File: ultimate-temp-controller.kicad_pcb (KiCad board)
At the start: 2 copper layers, 80 x 100 mm, 74 parts, among them CON1 SD_Card, IC1 ATMEGA328-A, P1 ISP, P10 RS485, P2 BUTTONS, P3 OPEN_DRAIN, P4 POWER, P5 I2C1, P6 I2C2, P7 CONN_01X05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

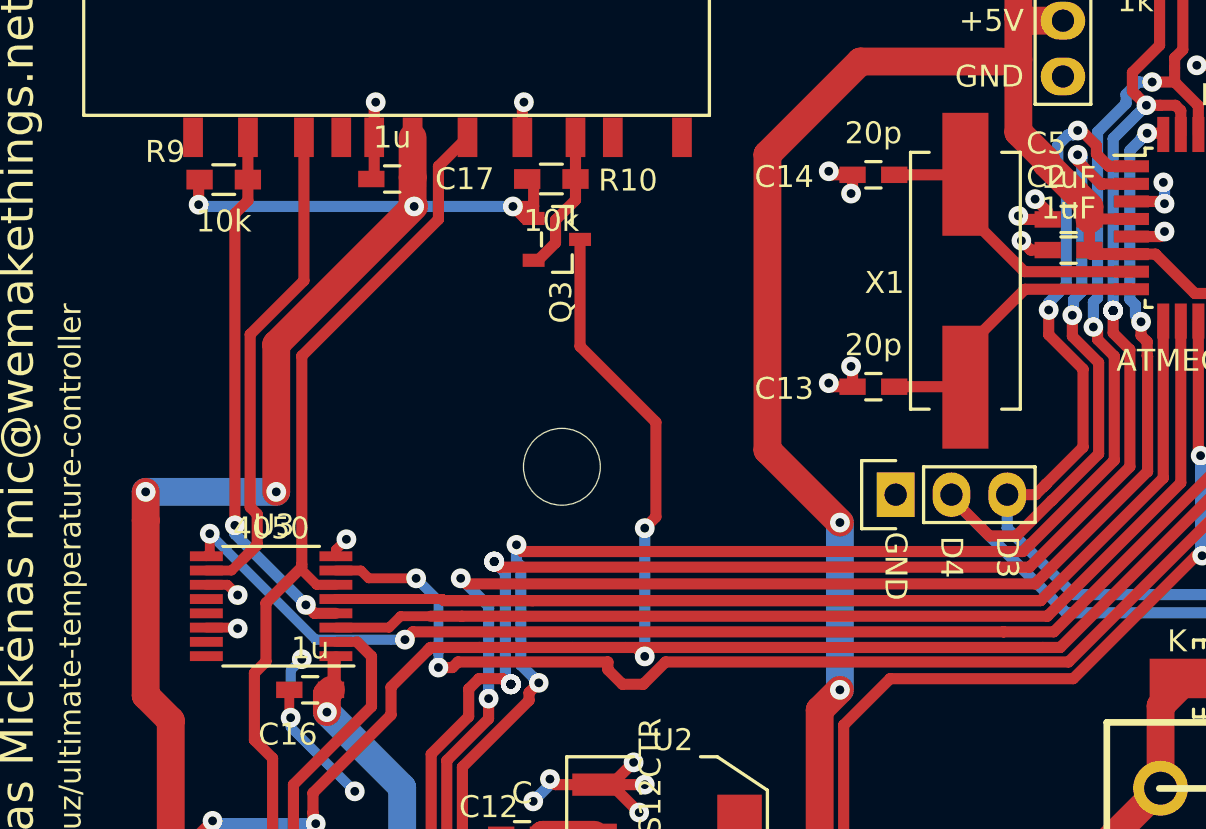
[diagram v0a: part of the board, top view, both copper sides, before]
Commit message: Optimise some tracks
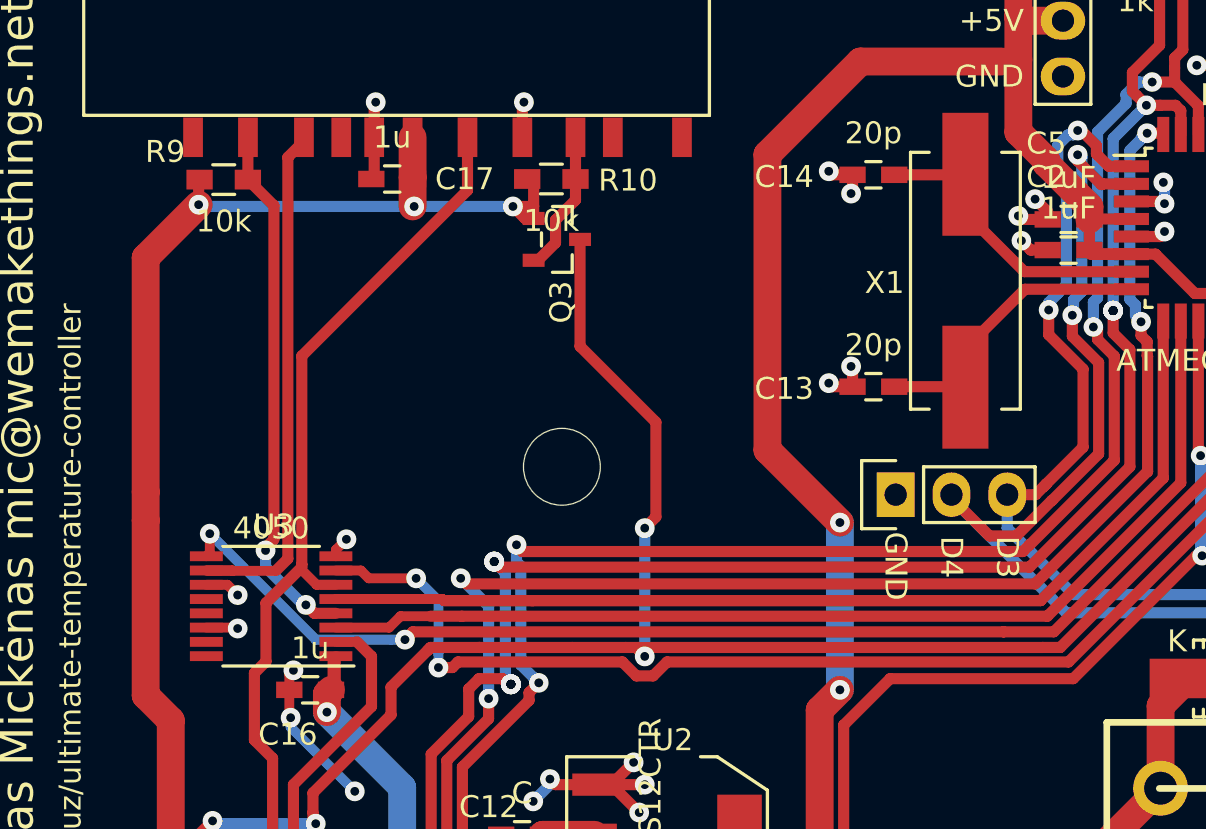
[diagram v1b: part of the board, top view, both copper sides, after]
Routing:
- net +3V3: track 128.1 -> 120.7 mm, vias 14 -> 12
- net /controller/MOSI_3V3: track 22.5 -> 24.6 mm
- net (no net): track 1.91 -> 0.00 mm, vias 1 -> 0
- net GND: track 78.8 -> 79.8 mm, vias 46 -> 47
- net /controller/CLK: track 66.0 -> 65.5 mm

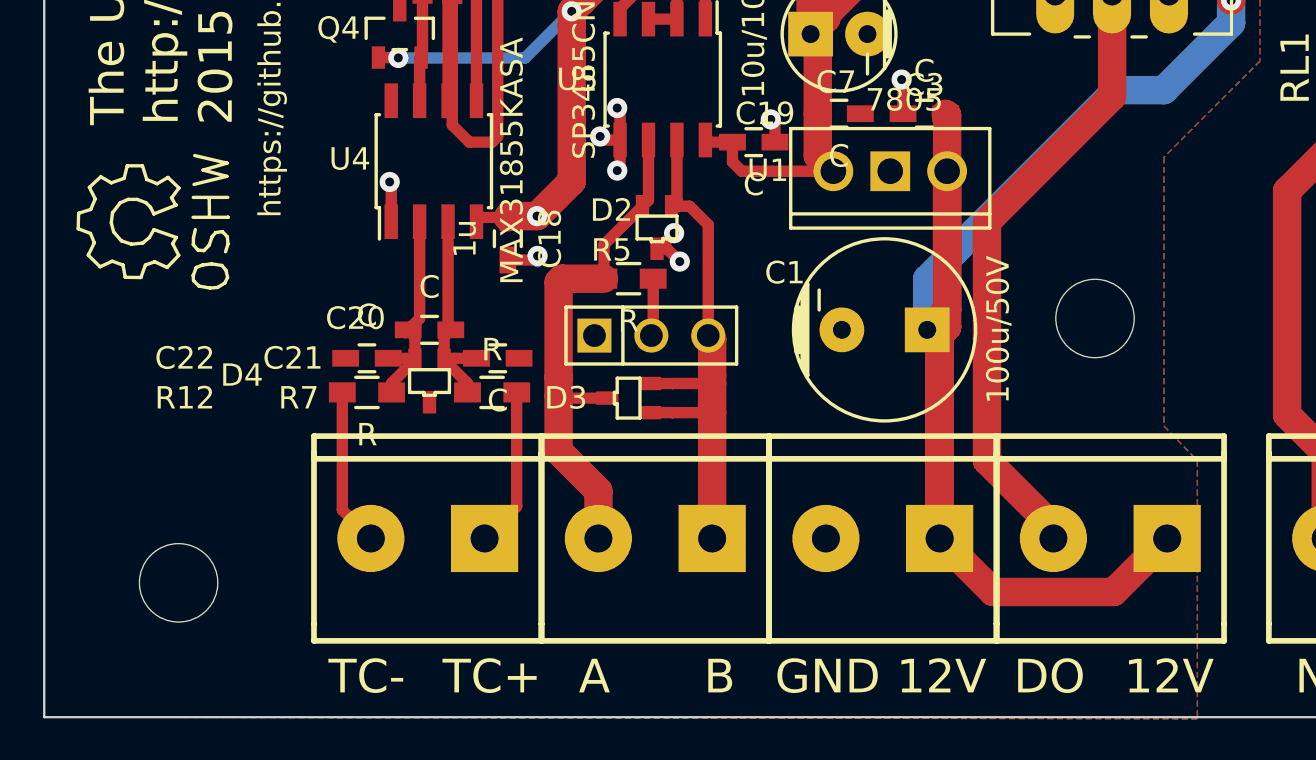
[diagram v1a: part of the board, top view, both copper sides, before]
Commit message: Change TVS diode footprints to SOT-23
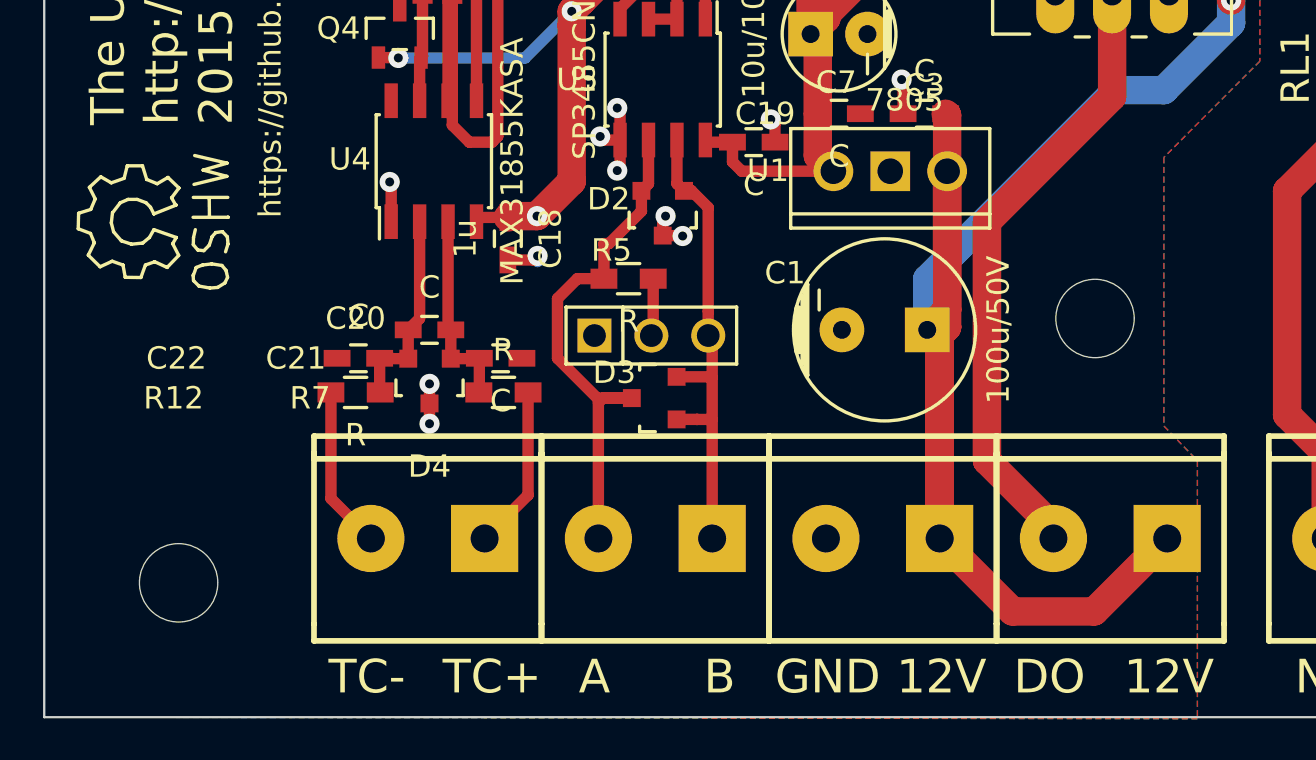
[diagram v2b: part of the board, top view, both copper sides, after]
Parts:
- D2, D3, D4: footprint SMD_Packages:SOT-323 -> Housings_SOT-23_SOT-143_TSOT-6:SOT-23
- moved D3 1.14 mm to (118.2, 174.8), turned to 90 degrees
- moved D2 0.68 mm to (118.6, 166.5), turned to 180 degrees
- moved R12 0.51 mm to (104.9, 174.5)
- moved R7 0.51 mm to (111.5, 174.5)
- moved C22 0.38 mm to (105.0, 173.0)
- moved C21 0.13 mm to (111.4, 173.0)
- turned D4 to 180 degrees
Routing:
- net /controller/RS485B: track 25.0 -> 21.8 mm
- net GND: track 79.8 -> 81.1 mm, vias 47 -> 49
- net Net-(C20-Pad1): track 9.71 -> 8.98 mm
- net VCC: track 88.6 -> 89.3 mm
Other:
- board text added: "TODO: -rezistorių ant CLK ir MOSI linijų? - patikrinti SD kortelės footprintą"
- board text removed: "TODO: - TVS diodu footprintai SC-70, tuo tarpu, kai nusipirkau sot-23 - pakeist MCU i 328P, kad būtų arduino -rezistorių ant CLK ir MOSI linijų? - patikrinti SD kortelės footprintą"

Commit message: Fix netlist problem - update custom tuded ICs: U3 power connections are visible, U5 pin ordering more convenient. Saved cymbol changes to the local cache, not clear if this will help thoug..
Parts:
- IC1: value ATMEGA328-A -> ATMEGA328P-A
- RLY1: renamed from RL1; value FINDER-40.51 -> RELAY_40.61
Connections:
- C1 pad 1: VCC -> +12V
- C3 pad 1: VCC -> +12V
- D1 pad 2: VCC -> +12V
- D4 pad 1: Net-(C20-Pad1) -> Net-(C20-Pad2)
- D4 pad 2: Net-(C20-Pad2) -> Net-(C20-Pad1)
- P3 pad 1: VCC -> +12V
- P4 pad 1: VCC -> +12V
- RLY1 pad 1: VCC -> Net-(D1-Pad1)
- RLY1 pad 2: Net-(D1-Pad1) -> +12V
- U1 pad VI: VCC -> +12V
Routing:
- net +12V: track 0.00 -> 89.3 mm, vias 0 -> 1
- net VCC: track 89.3 -> 0.00 mm, vias 1 -> 0
- net Net-(C20-Pad1): track 8.98 -> 7.72 mm
- net Net-(C20-Pad2): track 9.33 -> 10.6 mm

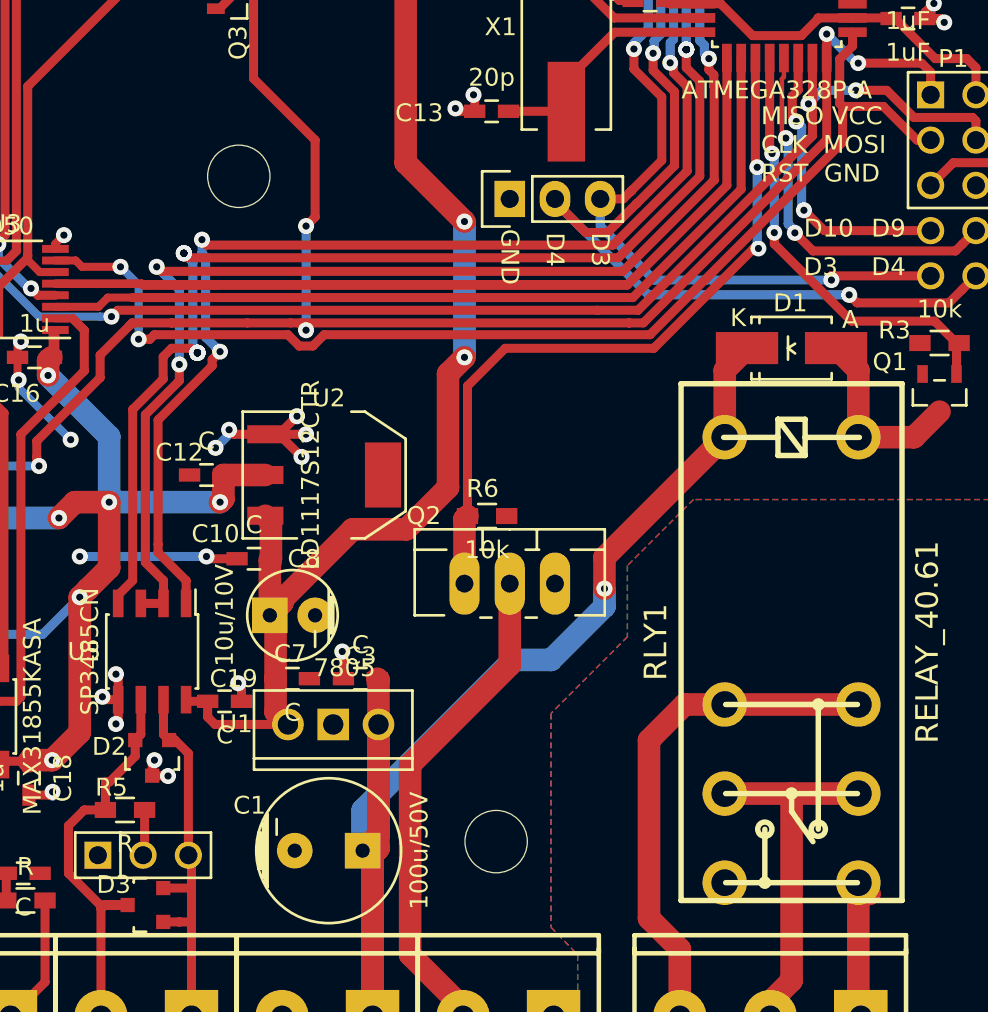
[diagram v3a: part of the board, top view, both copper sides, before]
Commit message: Swap TVS pins again. Add pullup resistors to CS lines.
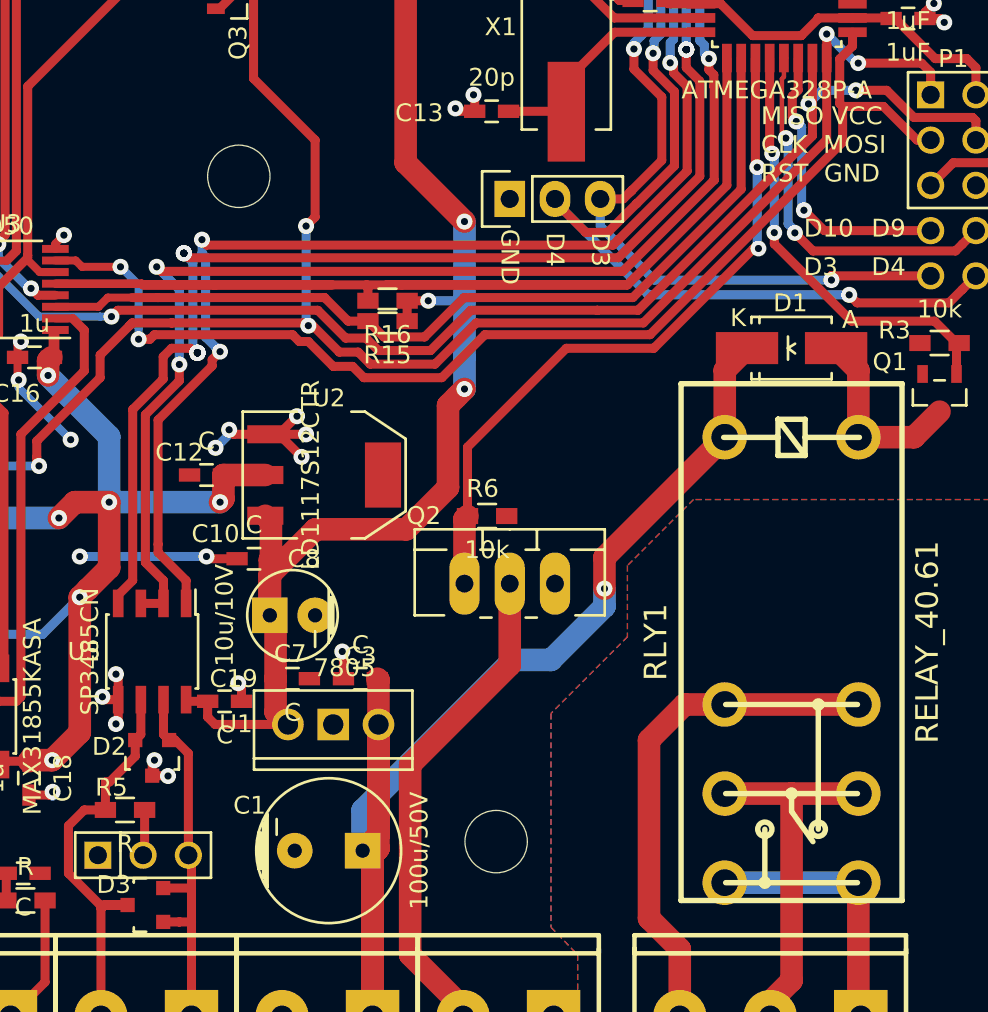
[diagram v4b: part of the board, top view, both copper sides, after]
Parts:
- added R15: 10k, Resistors_SMD:R_0603_HandSoldering, F.Cu at (131.8, 142.0)
- added R16: 10k, Resistors_SMD:R_0603_HandSoldering, F.Cu at (131.8, 140.8)
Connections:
- D4 pad 1: Net-(C20-Pad2) -> Net-(C20-Pad1)
- D4 pad 2: Net-(C20-Pad1) -> Net-(C20-Pad2)
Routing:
- net /controller/RELAY_NO: track 8.47 -> 15.3 mm
- net +5V: track 159.2 -> 164.8 mm, vias 2 -> 3
- net /controller/TRANSISTOR_ON: track 40.4 -> 38.4 mm
- net /controller/CS_SD: track 79.4 -> 77.4 mm
- net /controller/MOSI: track 72.0 -> 73.8 mm
- net /controller/CS_TC: track 48.6 -> 50.4 mm
- net /controller/CLK: track 65.5 -> 67.0 mm
- net Net-(C20-Pad1): track 7.72 -> 8.98 mm
- net Net-(C20-Pad2): track 10.6 -> 9.33 mm
- net /controller/MISO: track 105.9 -> 107.1 mm

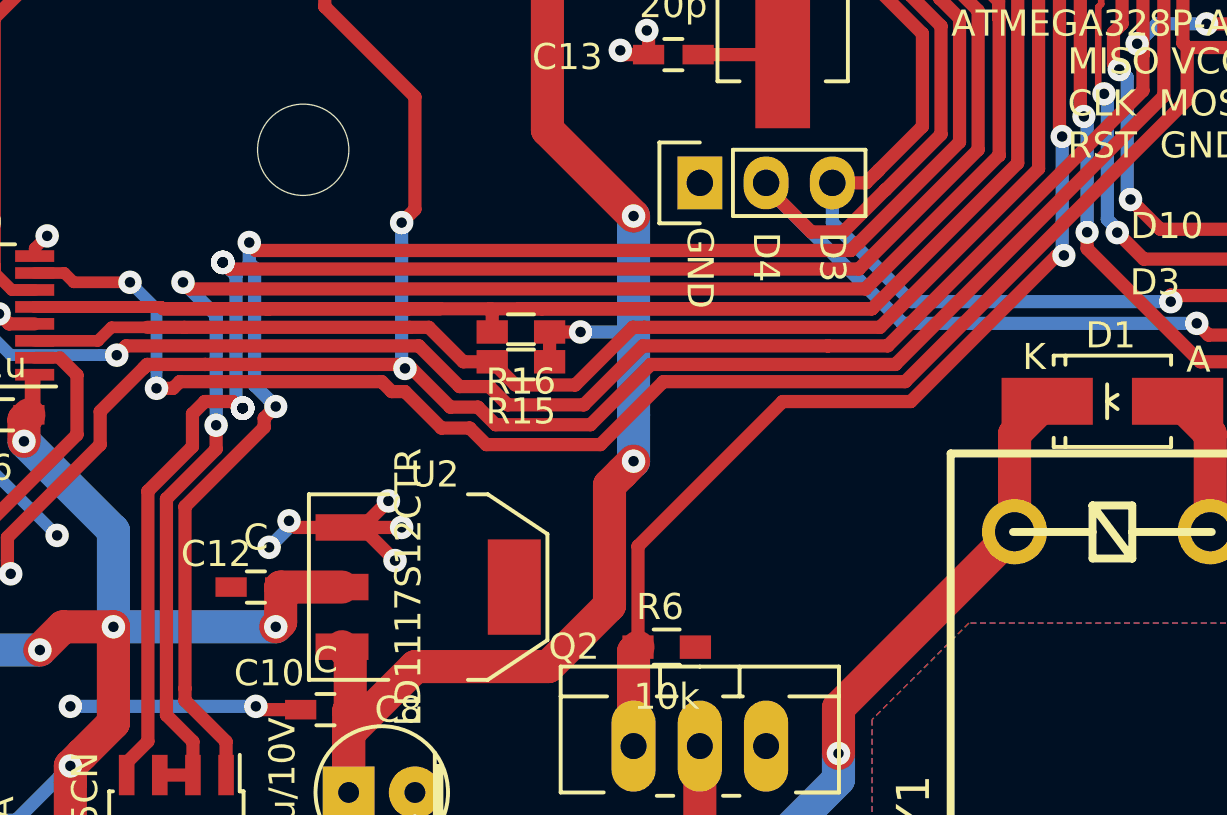
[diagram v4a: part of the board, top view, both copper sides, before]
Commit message: Optimise some tracks
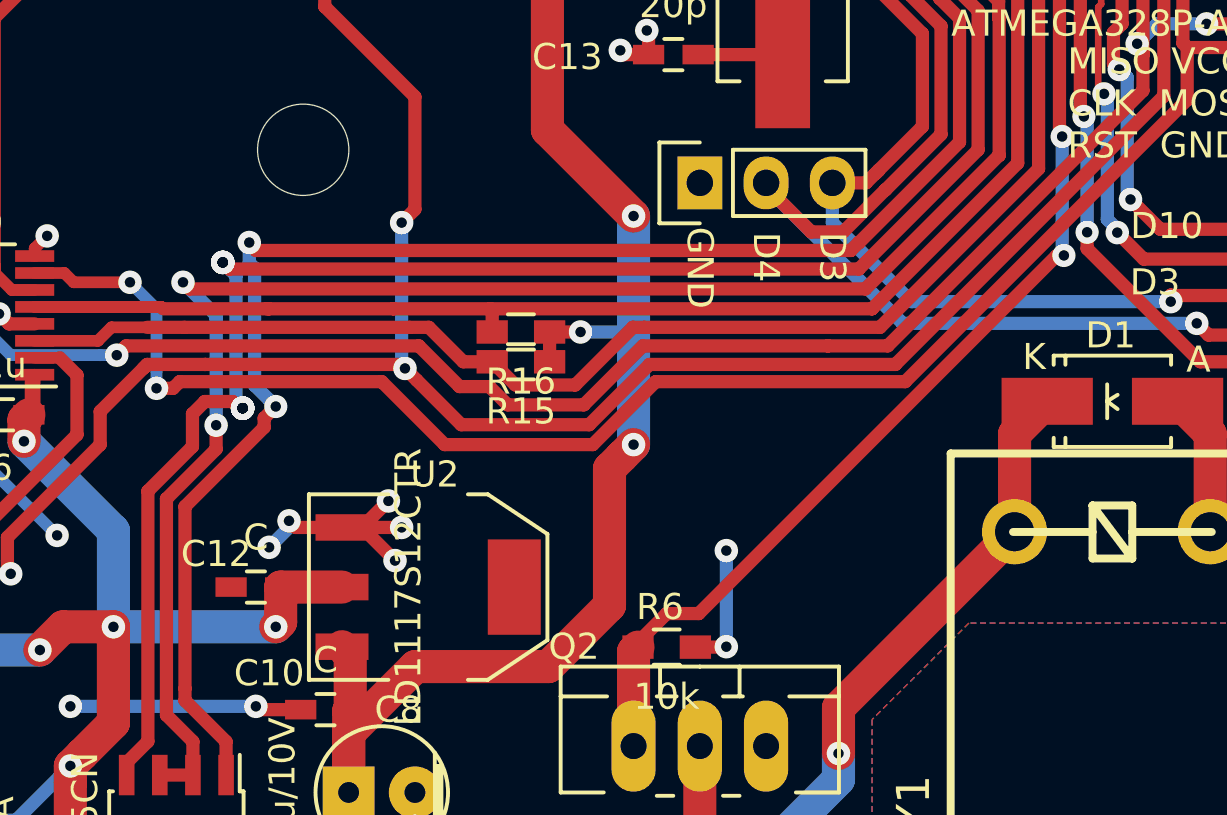
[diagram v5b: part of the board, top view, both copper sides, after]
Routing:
- net /controller/CS_SD: track 77.4 -> 53.3 mm
- net GND: track 81.1 -> 86.0 mm, vias 49 -> 51
- net /controller/TRANSISTOR_ON: track 38.4 -> 36.3 mm
